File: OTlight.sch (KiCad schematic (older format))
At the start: 66 parts, among them P1 CONN_01X01, Q1 TEMT6000, Q2 Q_NMOS_GSD, T1 TRANSFO, U1 LM3478, U10 IN-14, U11 IN-14, U12 MAX6931, U13 IN-14, U14 MAX6920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

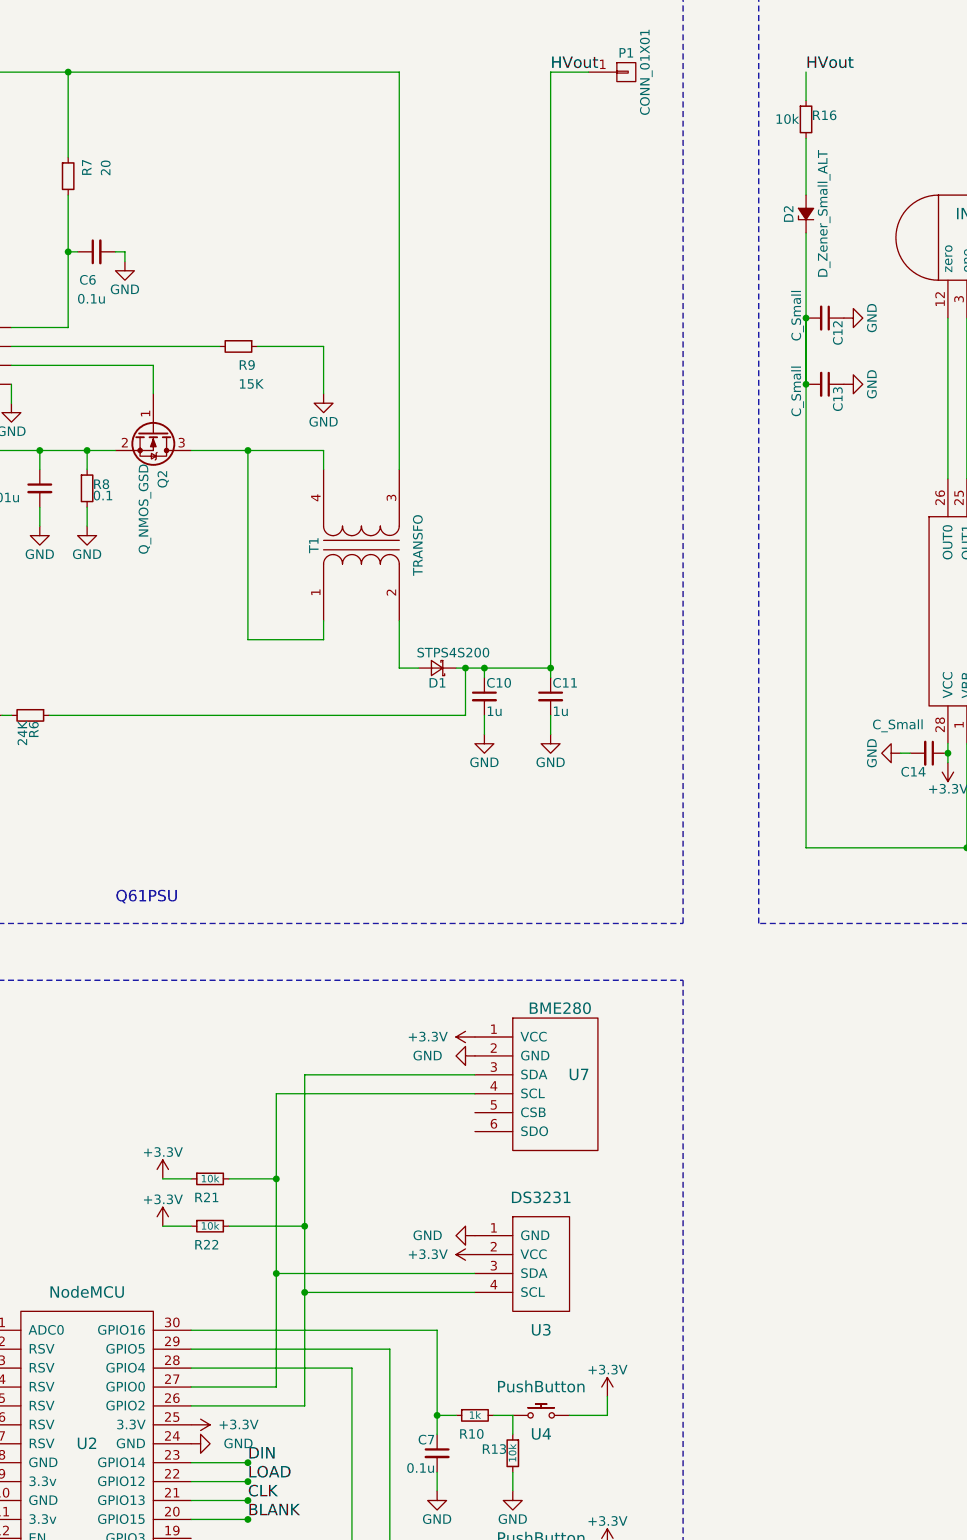
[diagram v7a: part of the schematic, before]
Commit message: Renamed components on schematics for more sensible name Also changed diode orientation and BME280 pinout
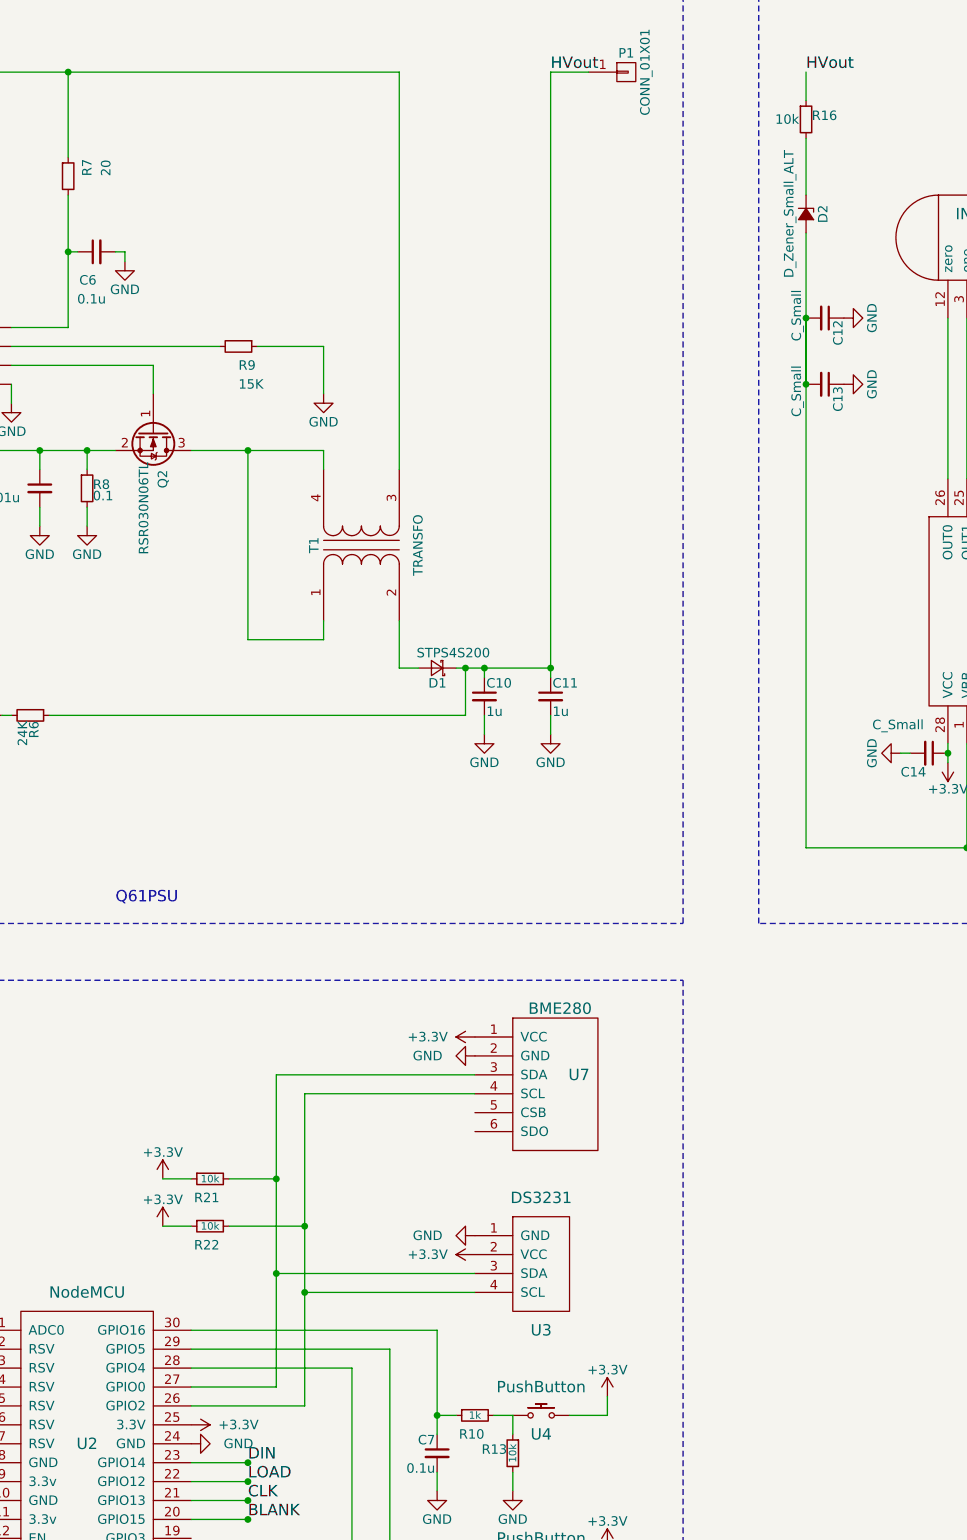
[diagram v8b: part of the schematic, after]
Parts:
- D1: footprint Diodes_SMD:D_SMB_Handsoldering -> Diodes_SMD:D_SMB-SMC_Universal_Handsoldering
- Q2: value Q_NMOS_GSD -> RSR030N06TL
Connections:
- net at C12.2, C13.2, U12.1 (VBB)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: now also D2.2 (A); no longer D2.1 (K)
- net at R16.2: now also D2.1 (K); no longer D2.2 (A)
- net at R22.2, U2.26 (GPIO2), U3.4 (SCL): now also U7.4 (SCL); no longer U7.3 (SDA)
- net at R21.2, U2.27 (GPIO0), U3.3 (SDA): now also U7.3 (SDA); no longer U7.4 (SCL)
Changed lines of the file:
@@
 LIBS:contrib
 LIBS:valves
+LIBS:bambouLab
 LIBS:OTlight-cache
 EELAYER 25 0
@@
 P 3650 2950
 F 0 "Q2" H 3950 3000 50  0000 R CNN
-F 1 "Q_NMOS_GSD" H 4300 2900 50  0000 R CNN
+F 1 "RSR030N06TL" H 4300 2900 50  0000 R CNN
 F 2 "TO_SOT_Packages_SMD:SOT-23_Handsoldering" H 3850 3050 50  0001 C CNN
 F 3 "" H 3650 2950 50  0000 C CNN
@@
 F 0 "D1" H 5100 4280 50  0000 L CNN
 F 1 "STPS4S200" H 4870 4120 50  0000 L CNN
-F 2 "Diodes_SMD:D_SMB_Handsoldering" V 5150 4200 50  0001 C CNN
+F 2 "Diodes_SMD:D_SMB-SMC_Universal_Handsoldering" V 5150 4200 50  0001 C CNN
 F 3 "" V 5150 4200 50  0000 C CNN
 	1    5150 4200
@@
 F 3 "" V 7100 1800 50  0000 C CNN
 	1    7100 1800
-	0    -1   -1   0
+	0    1    1    0
 $EndComp
 Text Label 8700 4700 3    60   ~ 0
@@
 	4300 8000 3850 8000
 Wire Wire Line
-	4300 6450 4300 8000
-Wire Wire Line
-	4300 6450 5350 6450
+	4300 6350 4300 8000
 Wire Wire Line
 	4450 8100 3850 8100
-Wire Wire Line
-	4450 6350 4450 8100
-Wire Wire Line
-	4450 6350 5350 6350
 Wire Wire Line
 	5350 7400 4300 7400
 Connection ~ 4300 7400
 Wire Wire Line
-	5350 7500 4450 7500
+	4450 7500 5350 7500
 Connection ~ 4450 7500
 Connection ~ 5150 8150
@@
 Connection ~ 7100 2350
 Connection ~ 7100 2700
+Wire Wire Line
+	4450 6450 4450 8100
+Wire Wire Line
+	5350 6450 4450 6450
+Wire Wire Line
+	5350 6350 4300 6350
 $EndSCHEMATC
